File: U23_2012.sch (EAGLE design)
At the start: 53 parts, among them X2 J1006F01P

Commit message: adds misc page
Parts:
- added C12, C13, C4: 100n, rcl:C-EU025-024X044
- added LED1, LED2, LED3, LED4, LED5: (no value), led:LED3MM
- added R24, R25, R26, R27, R28: 1k, rcl:R-EU_0207/10
- added R29, R30, R31, R32, R33, R34: 10k, rcl:R-EU_0207/10
- added S1, S2, S3, S4, S5, S6: (no value), switch-omron:10-XX
- added T1: BC337, transistor:BC337
- added TP1, TP2: TPTP20SQ, testpad:TPTP20SQ
- C1, C10, C11, C2, C5, C6, C7, C9: value 0.1µF -> 100n
- C3: value 0.01µF -> 10n; device rcl:CPOL-EUSMCC -> rcl:C-EUC0603
- C8: value 10µF -> 10u
- U$5: value (none) -> 50Mhz
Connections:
- removed net N$30: U$2.CARD_DETECT
- new net N$14: LED1.A, R24.1
- new net N$15: LED2.A, R25.1
- new net N$16: LED3.A, R26.1
- new net N$17: LED4.A, R27.1
- new net N$18: LED5.A, R28.1
- new net N$20: T1.C, TP1.TP
- net 3V: now also C3.2, C4.2, TP2.TP; no longer C3.+
- net 5V: now also C12.1, C13.1, R28.2, S1.S, S1.S1, S2.S, S2.S1, S3.S, S3.S1, S4.S, S4.S1, S5.S, S5.S1, S6.S, S6.S1
- net GND: now also C3.1, LED1.C, LED2.C, LED3.C, LED4.C, LED5.C, R29.1, R30.1, R31.1, R32.1, R33.1, R34.1, T1.E; no longer C3.-
- net PB0: now also R34.2, S6.P, S6.P1
- net PB1: now also R33.2, S5.P, S5.P1
- net PB2: now also U$2.CARD_DETECT
- net PB4: now also R29.2, S2.P, S2.P1
- net PB5: now also R31.2, S3.P, S3.P1
- net PB7: now also R30.2, S1.P, S1.P1
- net PB8: now also R32.2, S4.P, S4.P1
- net PD1: no longer U$4.LATCH
- net PD12: now also R24.2
- net PD13: now also R25.2
- net PD14: now also R26.2
- net PD15: now also R27.2
- net PD3: no longer U$4.CLOCK
- net PD6: now also U$4.LATCH
- net PD7: now also U$4.CLOCK
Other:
- note added: "A"
- note added: "B"
- note added: "DOWN"
- note added: "LEFT"
- note added: "RIGHT"
- note added: "UP"
- note removed: "WARNING: assign GPIO"

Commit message: removes pulldowns of buttons, due to internal pulldowns of MCU. Reexports netlist etc.
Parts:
- removed R29, R30, R31, R32, R33, R34: 10k, rcl:R-EU_0207/10
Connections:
- net GND: no longer R29.1, R30.1, R31.1, R32.1, R33.1, R34.1
- net PB0: no longer R34.2
- net PB1: no longer R33.2
- net PB4: no longer R29.2
- net PB5: no longer R31.2
- net PB7: no longer R30.2
- net PB8: no longer R32.2
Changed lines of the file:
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@@
 <part name="R28" library="rcl" deviceset="R-EU_" device="0207/10" value="1k"/>
 <part name="S2" library="switch-omron" deviceset="10-XX" device=""/>
-<part name="R29" library="rcl" deviceset="R-EU_" device="0207/10" value="10k"/>
 <part name="S1" library="switch-omron" deviceset="10-XX" device=""/>
-<part name="R30" library="rcl" deviceset="R-EU_" device="0207/10" value="10k"/>
 <part name="S3" library="switch-omron" deviceset="10-XX" device=""/>
-<part name="R31" library="rcl" deviceset="R-EU_" device="0207/10" value="10k"/>
 <part name="S4" library="switch-omron" deviceset="10-XX" device=""/>
-<part name="R32" library="rcl" deviceset="R-EU_" device="0207/10" value="10k"/>
 <part name="S5" library="switch-omron" deviceset="10-XX" device=""/>
-<part name="R33" library="rcl" deviceset="R-EU_" device="0207/10" value="10k"/>
 <part name="S6" library="switch-omron" deviceset="10-XX" device=""/>
-<part name="R34" library="rcl" deviceset="R-EU_" device="0207/10" value="10k"/>
 <part name="C4" library="rcl" deviceset="C-EU" device="025-024X044" value="100n"/>
 <part name="C12" library="rcl" deviceset="C-EU" device="025-024X044" value="100n"/>
@@
 <instance part="R28" gate="G$1" x="33.02" y="58.42" rot="R90"/>
 <instance part="S2" gate="1" x="121.92" y="116.84"/>
-<instance part="R29" gate="G$1" x="121.92" y="101.6" rot="R90"/>
 <instance part="S1" gate="1" x="101.6" y="93.98"/>
-<instance part="R30" gate="G$1" x="101.6" y="78.74" rot="R90"/>
 <instance part="S3" gate="1" x="121.92" y="78.74"/>
-<instance part="R31" gate="G$1" x="121.92" y="63.5" rot="R90"/>
 <instance part="S4" gate="1" x="142.24" y="93.98"/>
-<instance part="R32" gate="G$1" x="142.24" y="78.74" rot="R90"/>
 <instance part="S5" gate="1" x="231.14" y="116.84"/>
-<instance part="R33" gate="G$1" x="231.14" y="101.6" rot="R90"/>
 <instance part="S6" gate="1" x="195.58" y="83.82"/>
-<instance part="R34" gate="G$1" x="195.58" y="68.58" rot="R90"/>
 <instance part="T1" gate="G$1" x="162.56" y="137.16"/>
 <instance part="TP1" gate="G$1" x="165.1" y="152.4"/>
@@
 </segment>
 <segment>
-<pinref part="R29" gate="G$1" pin="1"/>
-<wire x1="121.92" y1="96.52" x2="121.92" y2="93.98" width="0.1524" layer="91"/>
-<label x="121.92" y="93.98" size="1.778" layer="95"/>
-</segment>
-<segment>
-<pinref part="R30" gate="G$1" pin="1"/>
-<wire x1="101.6" y1="73.66" x2="101.6" y2="71.12" width="0.1524" layer="91"/>
-<label x="101.6" y="71.12" size="1.778" layer="95"/>
-</segment>
-<segment>
-<pinref part="R31" gate="G$1" pin="1"/>
-<wire x1="121.92" y1="58.42" x2="121.92" y2="55.88" width="0.1524" layer="91"/>
-<label x="121.92" y="55.88" size="1.778" layer="95"/>
-</segment>
-<segment>
-<pinref part="R32" gate="G$1" pin="1"/>
-<wire x1="142.24" y1="73.66" x2="142.24" y2="71.12" width="0.1524" layer="91"/>
-<label x="142.24" y="71.12" size="1.778" layer="95"/>
-</segment>
-<segment>
-<pinref part="R33" gate="G$1" pin="1"/>
-<wire x1="231.14" y1="96.52" x2="231.14" y2="93.98" width="0.1524" layer="91"/>
-<label x="231.14" y="93.98" size="1.778" layer="95"/>
-</segment>
-<segment>
-<pinref part="R34" gate="G$1" pin="1"/>
-<wire x1="195.58" y1="63.5" x2="195.58" y2="60.96" width="0.1524" layer="91"/>
-<label x="195.58" y="60.96" size="1.778" layer="95"/>
-</segment>
-<segment>
 <pinref part="T1" gate="G$1" pin="E"/>
 <wire x1="165.1" y1="132.08" x2="165.1" y2="124.46" width="0.1524" layer="91"/>
@@
 <wire x1="101.6" y1="88.9" x2="104.14" y2="88.9" width="0.1524" layer="91"/>
 <wire x1="101.6" y1="88.9" x2="101.6" y2="86.36" width="0.1524" layer="91"/>
-<pinref part="R30" gate="G$1" pin="2"/>
-<wire x1="101.6" y1="86.36" x2="101.6" y2="83.82" width="0.1524" layer="91"/>
 <wire x1="101.6" y1="86.36" x2="104.14" y2="86.36" width="0.1524" layer="91"/>
 <label x="104.14" y="86.36" size="1.778" layer="95"/>
-<junction x="101.6" y="86.36"/>
 <junction x="104.14" y="88.9"/>
 <junction x="101.6" y="88.9"/>
@@
 <wire x1="195.58" y1="78.74" x2="198.12" y2="78.74" width="0.1524" layer="91"/>
 <wire x1="195.58" y1="78.74" x2="195.58" y2="76.2" width="0.1524" layer="91"/>
-<pinref part="R34" gate="G$1" pin="2"/>
-<wire x1="195.58" y1="76.2" x2="195.58" y2="73.66" width="0.1524" layer="91"/>
 <wire x1="195.58" y1="76.2" x2="198.12" y2="76.2" width="0.1524" layer="91"/>
 <label x="198.12" y="76.2" size="1.778" layer="95"/>
-<junction x="195.58" y="76.2"/>
 <junction x="198.12" y="78.74"/>
 <junction x="195.58" y="78.74"/>
@@
 <wire x1="231.14" y1="111.76" x2="233.68" y2="111.76" width="0.1524" layer="91"/>
 <wire x1="231.14" y1="111.76" x2="231.14" y2="109.22" width="0.1524" layer="91"/>
-<pinref part="R33" gate="G$1" pin="2"/>
-<wire x1="231.14" y1="109.22" x2="231.14" y2="106.68" width="0.1524" layer="91"/>
 <wire x1="231.14" y1="109.22" x2="233.68" y2="109.22" width="0.1524" layer="91"/>
 <label x="233.68" y="109.22" size="1.778" layer="95"/>
-<junction x="231.14" y="109.22"/>
 <junction x="233.68" y="111.76"/>
 <junction x="231.14" y="111.76"/>
@@
 <wire x1="121.92" y1="111.76" x2="124.46" y2="111.76" width="0.1524" layer="91"/>
 <wire x1="121.92" y1="111.76" x2="121.92" y2="109.22" width="0.1524" layer="91"/>
-<pinref part="R29" gate="G$1" pin="2"/>
-<wire x1="121.92" y1="109.22" x2="121.92" y2="106.68" width="0.1524" layer="91"/>
 <wire x1="121.92" y1="109.22" x2="124.46" y2="109.22" width="0.1524" layer="91"/>
 <label x="124.46" y="109.22" size="1.778" layer="95"/>
-<junction x="121.92" y="109.22"/>
 <junction x="124.46" y="111.76"/>
 <junction x="121.92" y="111.76"/>
@@
 <wire x1="121.92" y1="73.66" x2="124.46" y2="73.66" width="0.1524" layer="91"/>
 <wire x1="121.92" y1="73.66" x2="121.92" y2="71.12" width="0.1524" layer="91"/>
-<pinref part="R31" gate="G$1" pin="2"/>
-<wire x1="121.92" y1="71.12" x2="121.92" y2="68.58" width="0.1524" layer="91"/>
 <wire x1="121.92" y1="71.12" x2="124.46" y2="71.12" width="0.1524" layer="91"/>
 <label x="124.46" y="71.12" size="1.778" layer="95"/>
-<junction x="121.92" y="71.12"/>
 <junction x="124.46" y="73.66"/>
 <junction x="121.92" y="73.66"/>
@@
 <wire x1="142.24" y1="88.9" x2="144.78" y2="88.9" width="0.1524" layer="91"/>
 <wire x1="142.24" y1="88.9" x2="142.24" y2="86.36" width="0.1524" layer="91"/>
-<pinref part="R32" gate="G$1" pin="2"/>
-<wire x1="142.24" y1="86.36" x2="142.24" y2="83.82" width="0.1524" layer="91"/>
 <wire x1="142.24" y1="86.36" x2="144.78" y2="86.36" width="0.1524" layer="91"/>
 <label x="144.78" y="86.36" size="1.778" layer="95"/>
-<junction x="142.24" y="86.36"/>
 <junction x="144.78" y="88.9"/>
 <junction x="142.24" y="88.9"/>

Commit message: adds missing base resistor to T1
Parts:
- added R29: 270, rcl:R-EU_0207/10
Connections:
- new net N$19: R29.2, T1.B
- net PD8: now also R29.1
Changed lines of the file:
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@@
 <part name="TP1" library="testpad" deviceset="TP" device="TP20SQ"/>
 <part name="TP2" library="testpad" deviceset="TP" device="TP20SQ"/>
+<part name="R29" library="rcl" deviceset="R-EU_" device="0207/10" value="270"/>
 </parts>
 <sheets>
@@
 <instance part="TP1" gate="G$1" x="165.1" y="152.4"/>
 <instance part="TP2" gate="G$1" x="165.1" y="154.94" rot="R180"/>
+<instance part="R29" gate="G$1" x="154.94" y="137.16"/>
 </instances>
 <busses>
@@
 </segment>
 </net>
+<net name="N$19" class="0">
+<segment>
+<pinref part="T1" gate="G$1" pin="B"/>
+<pinref part="R29" gate="G$1" pin="2"/>
+</segment>
+</net>
+<net name="PD8" class="0">
+<segment>
+<pinref part="R29" gate="G$1" pin="1"/>
+<wire x1="149.86" y1="137.16" x2="142.24" y2="137.16" width="0.1524" layer="91"/>
+<label x="142.24" y="137.16" size="1.778" layer="95"/>
+</segment>
+</net>

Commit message: board rev 0.1
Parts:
- removed U$10, U$11, U$12, U$13, U$14, U$6, U$7, U$8, U$9: DO_WHAT_I_WANT, library:DO_WHAT_I_WANT
- RN1, RN2: device resistor-dil:4R-N0603-ARV -> resistor-dil:4R-N
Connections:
- removed net CRS_DV: R16.1, U$1.CRS/CRS_DV/LED_CFG, U$8.1
- removed net MDC: U$1.MDC, U$9.1
- removed net MDIO: U$1.MDIO, U$7.1
- removed net OSCIN: U$1.X1, U$5.OUT, U$6.1
- removed net RXD0: U$1.RXD_0/PHYAD1, U$10.1
- removed net RXD1: U$1.RXD_1/PHYAD2, U$11.1
- removed net TXD0: U$1.TXD_0, U$13.1
- removed net TXD1: U$1.TXD_1, U$14.1
- removed net TX_EN: U$1.TX_EN, U$12.1
- net GND: now also C12.2, C13.2, C4.1, R9.2
- net PA1: now also U$1.X1, U$5.OUT; no longer U$6.2
- net PA2: now also U$1.MDIO; no longer U$7.2
- net PA7: now also R16.1, U$1.CRS/CRS_DV/LED_CFG; no longer U$8.2
- net PB11: now also U$1.TX_EN; no longer U$12.2
- net PB12: now also U$1.TXD_0; no longer U$13.2
- net PB13: now also U$1.TXD_1; no longer U$14.2
- net PC1: now also U$1.MDC; no longer U$9.2
- net PC4: now also U$1.RXD_0/PHYAD1; no longer U$10.2
- net PC5: now also U$1.RXD_1/PHYAD2; no longer U$11.2

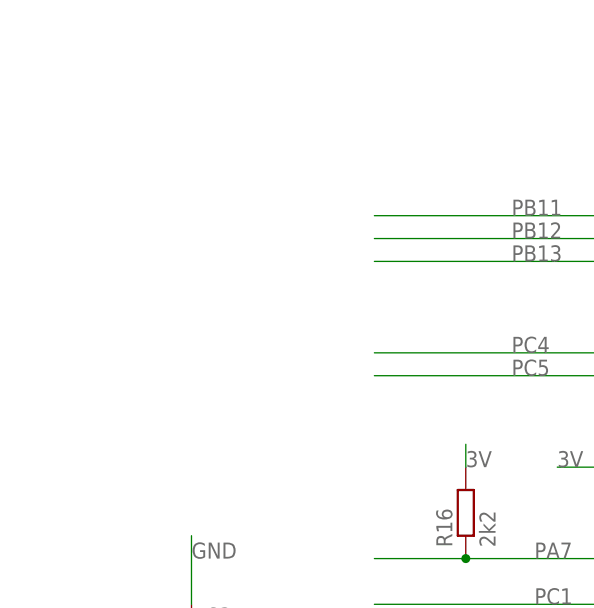
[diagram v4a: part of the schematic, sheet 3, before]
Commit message: adds connector to http://www.wvshare.com/product/DP83848-Ethernet-Board.htm Ethernet boards switches position of LED1 and LED5 adds silkscreen annotations etc removes pdf and drill files
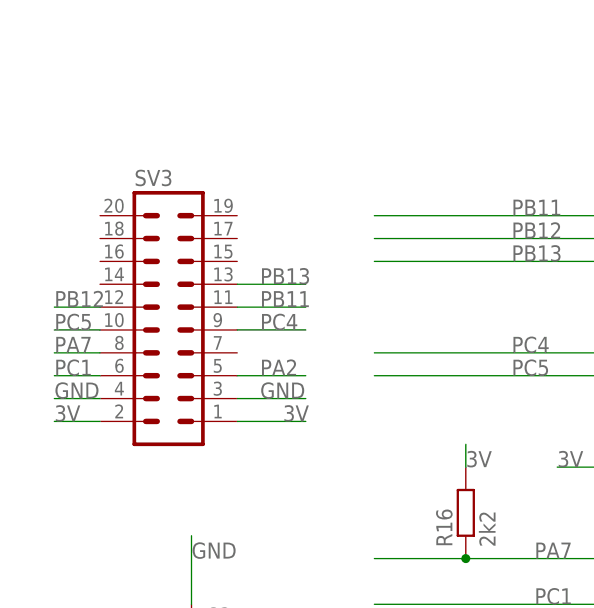
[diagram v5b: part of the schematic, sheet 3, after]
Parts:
- added SV3: (no value), con-harting-ml:ML20L
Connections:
- net 3V: now also SV3.1, SV3.2
- net GND: now also SV3.3, SV3.4
- net PA2: now also SV3.5
- net PA7: now also SV3.8
- net PB11: now also SV3.11
- net PB12: now also SV3.12
- net PB13: now also SV3.13
- net PC1: now also SV3.6
- net PC4: now also SV3.9
- net PC5: now also SV3.10

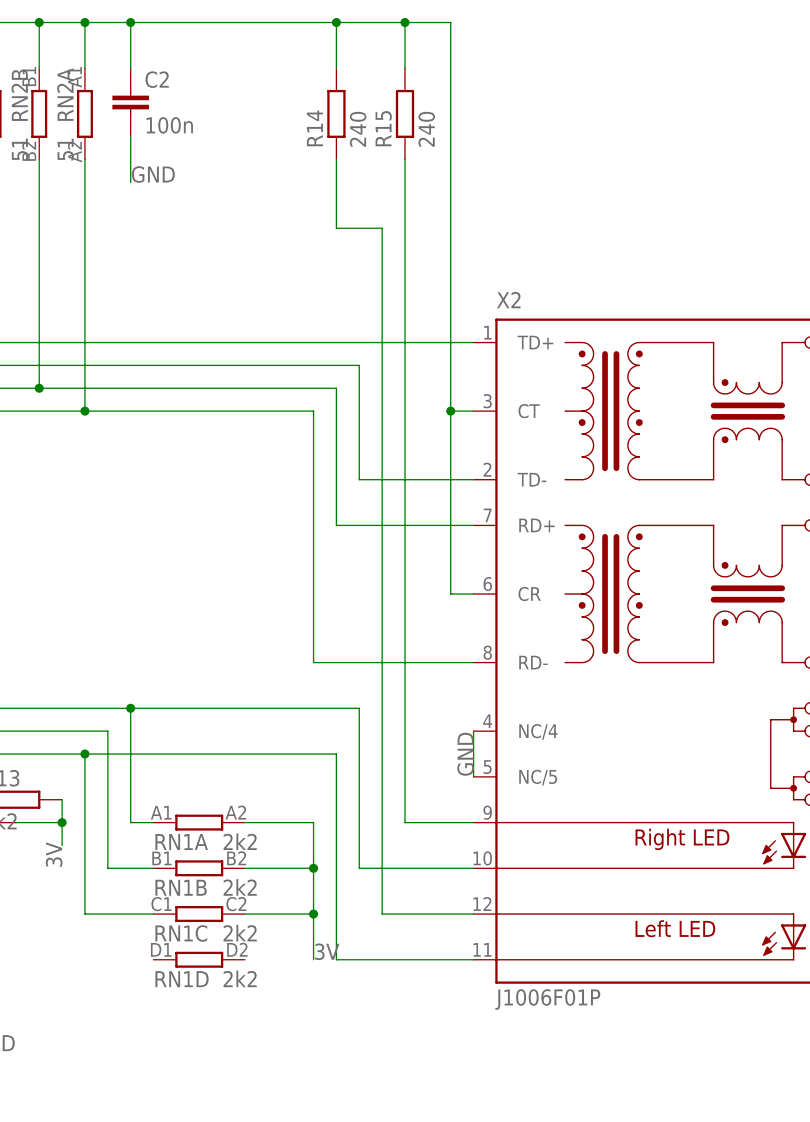
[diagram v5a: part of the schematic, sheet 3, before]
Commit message: removes stupid mistake on ethernet jack
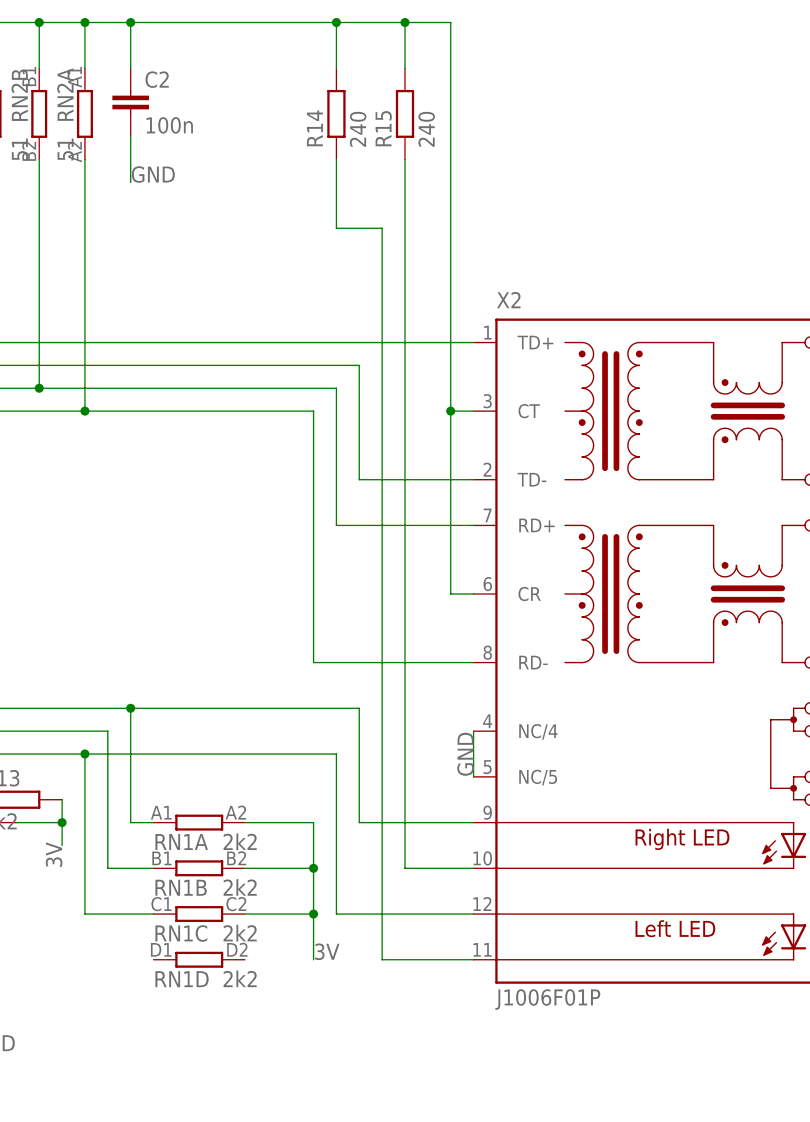
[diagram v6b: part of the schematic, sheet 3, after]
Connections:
- net N$12: now also X2.C-R; no longer X2.A-R
- net N$13: now also X2.C-L; no longer X2.A-L
- net N$5: now also X2.A-R; no longer X2.C-R
- net N$6: now also X2.A-L; no longer X2.C-L
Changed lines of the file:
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@@
 <?xml version="1.0" encoding="utf-8"?>
 <!DOCTYPE eagle SYSTEM "eagle.dtd">
-<eagle version="6.2">
+<eagle version="6.3">
 <drawing>
 <settings>
@@
 <wire x1="96.52" y1="71.12" x2="119.38" y2="71.12" width="0.1524" layer="91"/>
 <wire x1="119.38" y1="71.12" x2="144.78" y2="71.12" width="0.1524" layer="91"/>
-<wire x1="144.78" y1="71.12" x2="144.78" y2="53.34" width="0.1524" layer="91"/>
-<pinref part="X2" gate="G$1" pin="C-R"/>
-<wire x1="144.78" y1="53.34" x2="157.48" y2="53.34" width="0.1524" layer="91"/>
 <wire x1="119.38" y1="71.12" x2="119.38" y2="58.42" width="0.1524" layer="91"/>
 <junction x="119.38" y="71.12"/>
 <pinref part="RN1" gate="A" pin="1"/>
 <wire x1="119.38" y1="58.42" x2="121.92" y2="58.42" width="0.1524" layer="91"/>
+<wire x1="144.78" y1="71.12" x2="144.78" y2="58.42" width="0.1524" layer="91"/>
+<pinref part="X2" gate="G$1" pin="A-R"/>
+<wire x1="144.78" y1="58.42" x2="157.48" y2="58.42" width="0.1524" layer="91"/>
 </segment>
 </net>
@@
 <wire x1="96.52" y1="66.04" x2="114.3" y2="66.04" width="0.1524" layer="91"/>
 <wire x1="114.3" y1="66.04" x2="142.24" y2="66.04" width="0.1524" layer="91"/>
-<wire x1="142.24" y1="66.04" x2="142.24" y2="43.18" width="0.1524" layer="91"/>
-<pinref part="X2" gate="G$1" pin="C-L"/>
-<wire x1="142.24" y1="43.18" x2="157.48" y2="43.18" width="0.1524" layer="91"/>
 <wire x1="114.3" y1="66.04" x2="114.3" y2="48.26" width="0.1524" layer="91"/>
 <junction x="114.3" y="66.04"/>
 <pinref part="RN1" gate="C" pin="1"/>
 <wire x1="114.3" y1="48.26" x2="121.92" y2="48.26" width="0.1524" layer="91"/>
+<wire x1="142.24" y1="66.04" x2="142.24" y2="48.26" width="0.1524" layer="91"/>
+<pinref part="X2" gate="G$1" pin="A-L"/>
+<wire x1="142.24" y1="48.26" x2="157.48" y2="48.26" width="0.1524" layer="91"/>
 </segment>
 </net>
@@
 <segment>
 <pinref part="R15" gate="G$1" pin="1"/>
-<wire x1="149.86" y1="132.08" x2="149.86" y2="58.42" width="0.1524" layer="91"/>
-<pinref part="X2" gate="G$1" pin="A-R"/>
-<wire x1="149.86" y1="58.42" x2="157.48" y2="58.42" width="0.1524" layer="91"/>
+<wire x1="149.86" y1="132.08" x2="149.86" y2="53.34" width="0.1524" layer="91"/>
+<pinref part="X2" gate="G$1" pin="C-R"/>
+<wire x1="149.86" y1="53.34" x2="157.48" y2="53.34" width="0.1524" layer="91"/>
 </segment>
 </net>
@@
 <wire x1="142.24" y1="132.08" x2="142.24" y2="124.46" width="0.1524" layer="91"/>
 <wire x1="142.24" y1="124.46" x2="147.32" y2="124.46" width="0.1524" layer="91"/>
-<wire x1="147.32" y1="124.46" x2="147.32" y2="48.26" width="0.1524" layer="91"/>
-<pinref part="X2" gate="G$1" pin="A-L"/>
-<wire x1="147.32" y1="48.26" x2="157.48" y2="48.26" width="0.1524" layer="91"/>
-</segment>
-</net>
+<wire x1="147.32" y1="124.46" x2="147.32" y2="43.18" width="0.1524" layer="91"/>
+<pinref part="X2" gate="G$1" pin="C-L"/>
+<wire x1="147.32" y1="43.18" x2="157.48" y2="43.18" width="0.1524" layer="91"/>
+</segment>
+</net>
